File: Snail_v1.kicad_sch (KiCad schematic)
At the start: 18 parts, among them J1 PWM_Connector, U1 PAM8406D, U2 STM32G431K6Tx

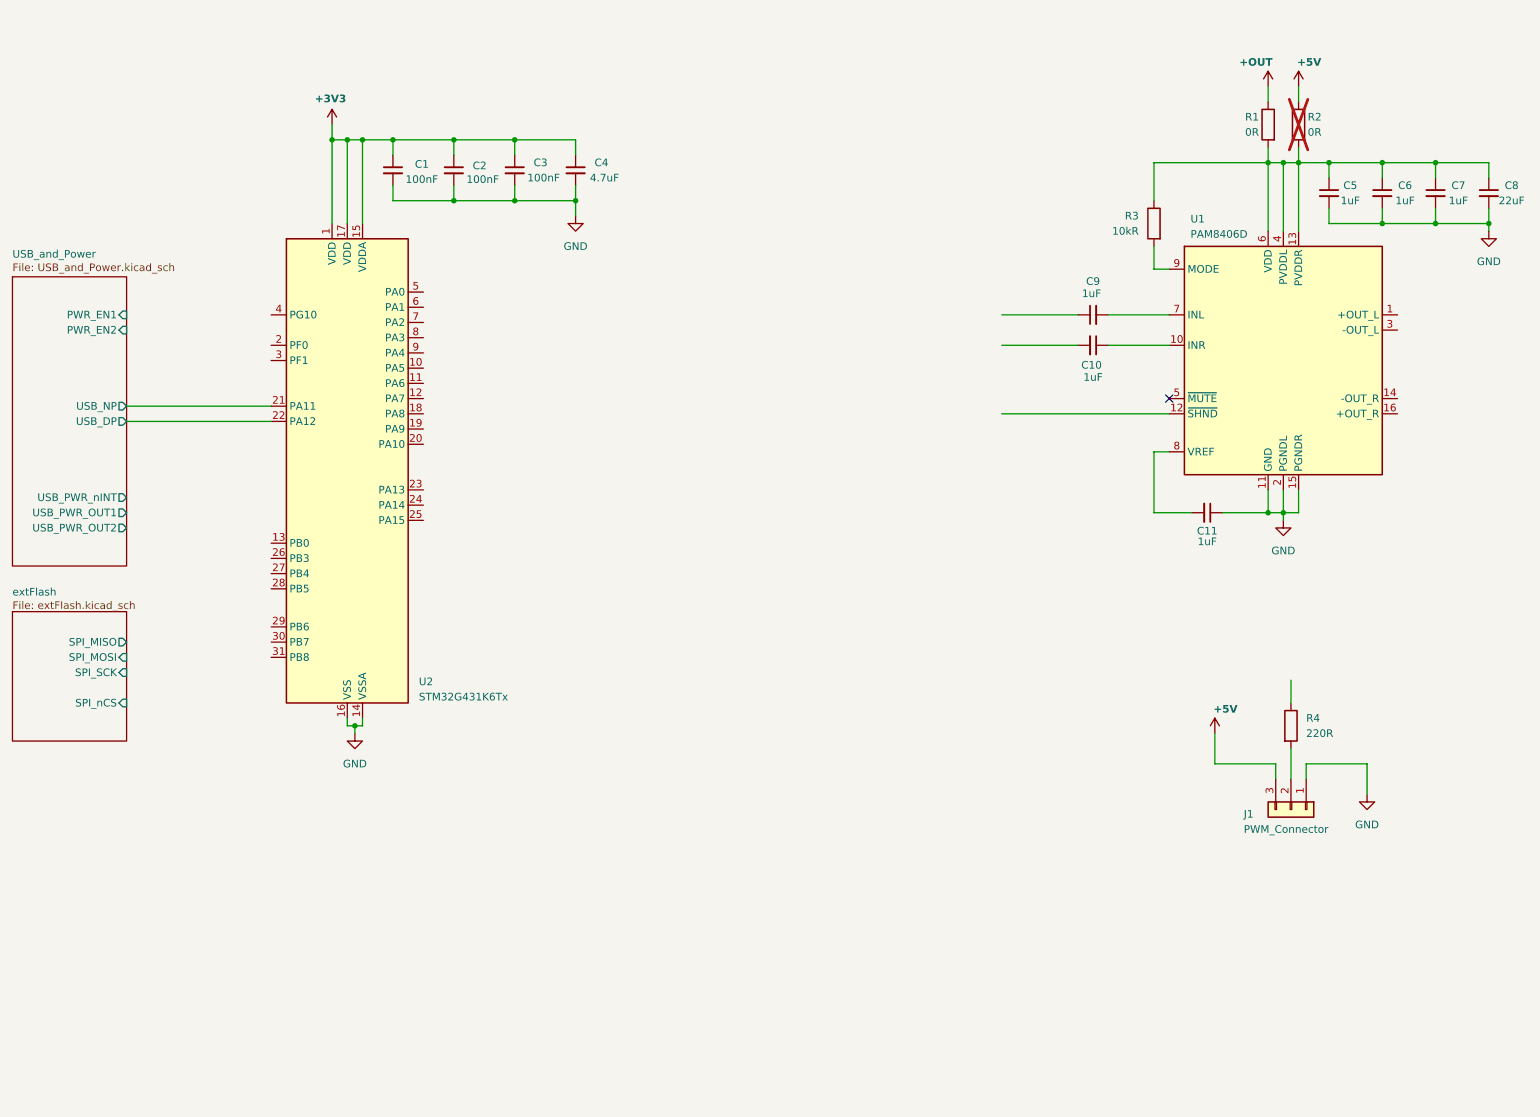
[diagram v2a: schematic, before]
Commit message: Added JDY-68A and replaced Amp-IC for PAM8302AAS
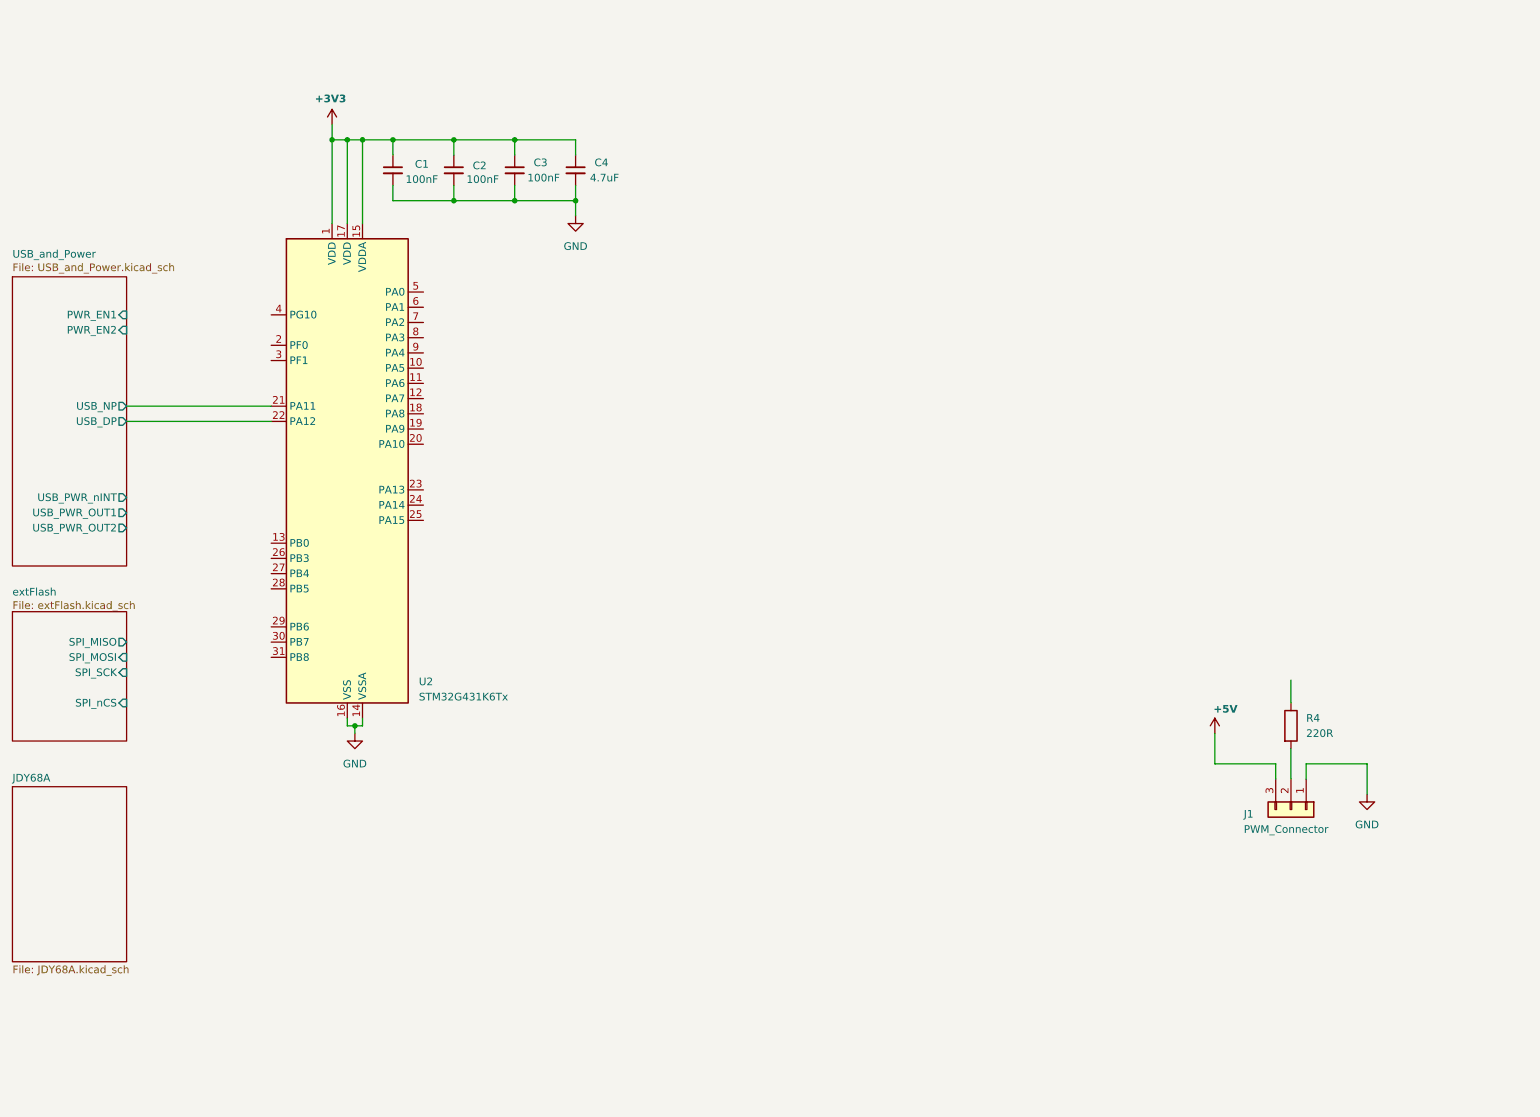
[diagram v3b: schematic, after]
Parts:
- removed C10, C11, C5, C6, C7, C9: 1uF, symbol Device:C_Small
- removed C8: 22uF, symbol Device:C_Small
- removed R1, R2: 0R, symbol Device:R
- removed R3: 10kR, symbol Device:R
- removed U1: PAM8406D, Package_SO:SOIC-16_3.9x9.9mm_P1.27mm, symbol Amplifier_Audio:PAM8406D
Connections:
- no-connect marks 1 -> 0
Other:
- added sheet JDY68A (JDY68A.kicad_sch)

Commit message: Changed LDO to Buc-Boost
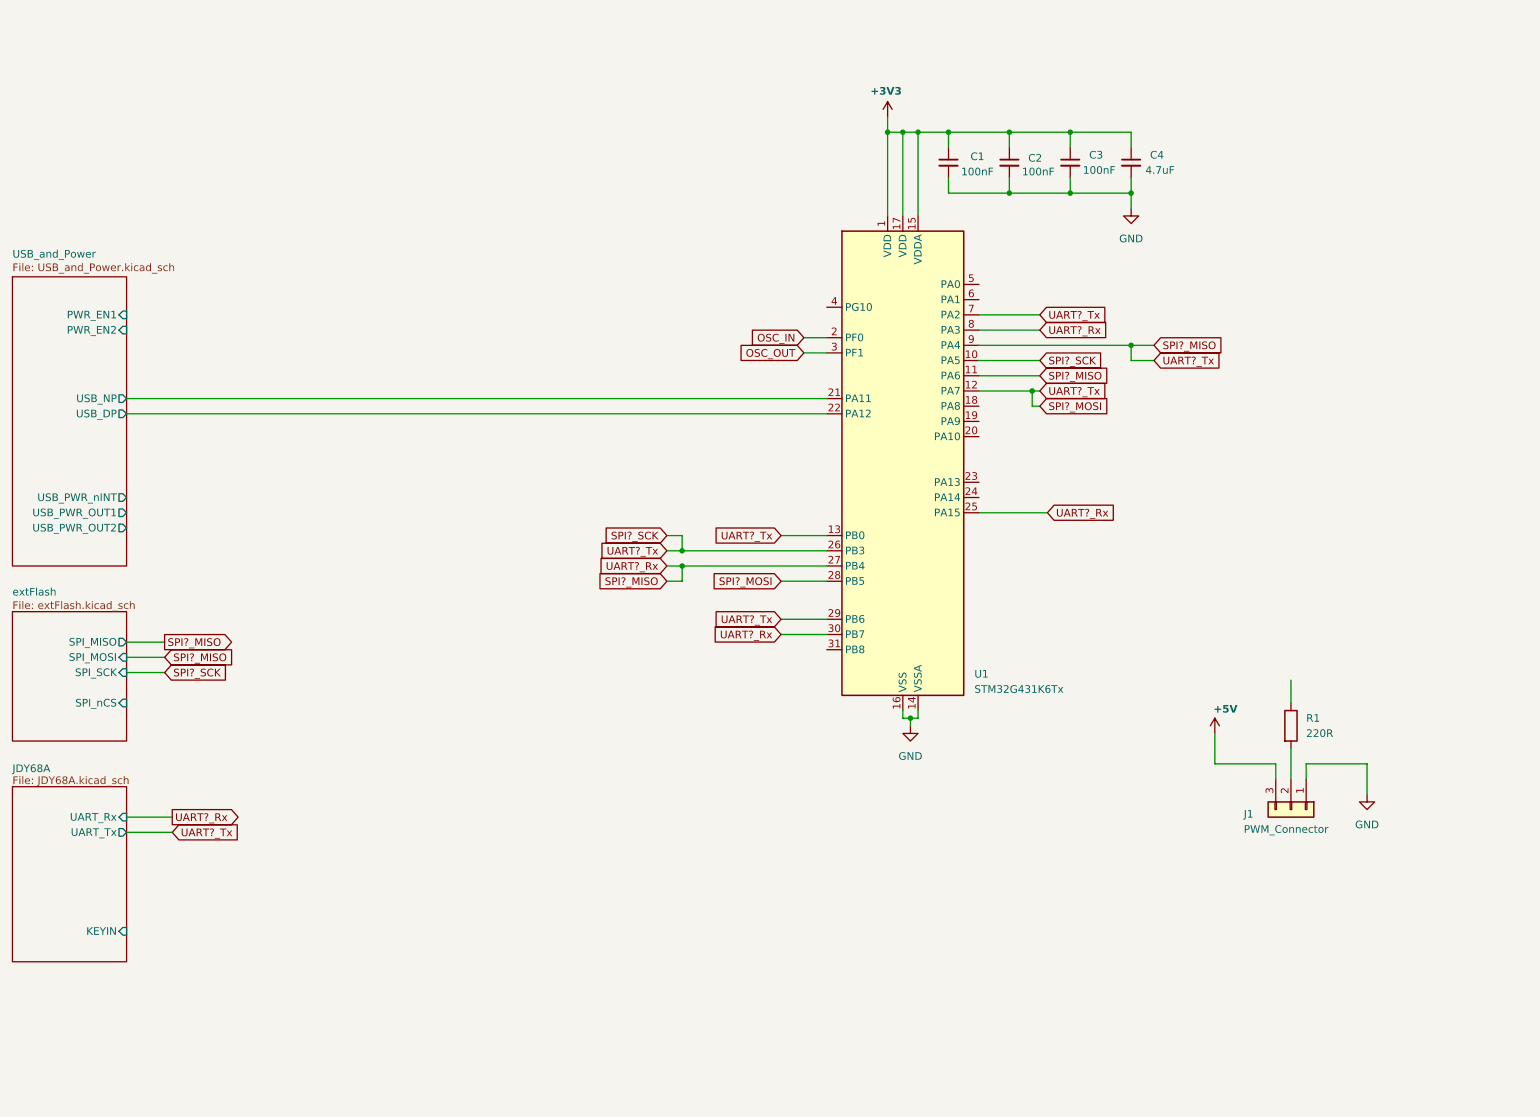
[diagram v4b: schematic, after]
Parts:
- C1, C2, C3, C4: footprint (none) -> Capacitor_SMD:C_0805_2012Metric_Pad1.18x1.45mm_HandSolder
- J1: footprint (none) -> Connector_PinHeader_2.54mm:PinHeader_1x03_P2.54mm_Vertical
- R1: renamed from R4; footprint (none) -> Resistor_SMD:R_0805_2012Metric_Pad1.20x1.40mm_HandSolder
- renumbered U2 to U1
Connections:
- net SPI?_MISO: now reaches U1.10 (PA5)
- net SPI?_MISO: now also U1.11 (PA6), U1.12 (PA7), U1.13 (PB0), U1.25 (PA15), U1.26 (PB3), U1.27 (PB4), U1.28 (PB5), U1.29 (PB6), U1.30 (PB7), U1.7 (PA2), U1.8 (PA3), U1.9 (PA4)
- net OSC_IN: now reaches U1.2 (PF0)
- net OSC_OUT: now reaches U1.3 (PF1)
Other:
- sheet JDY68A ports: added KEYIN, UART_Rx, UART_Tx; removed none
- moved on the sheet: C1, C2, C3, C4, U1

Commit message: Added LEDs + TPs
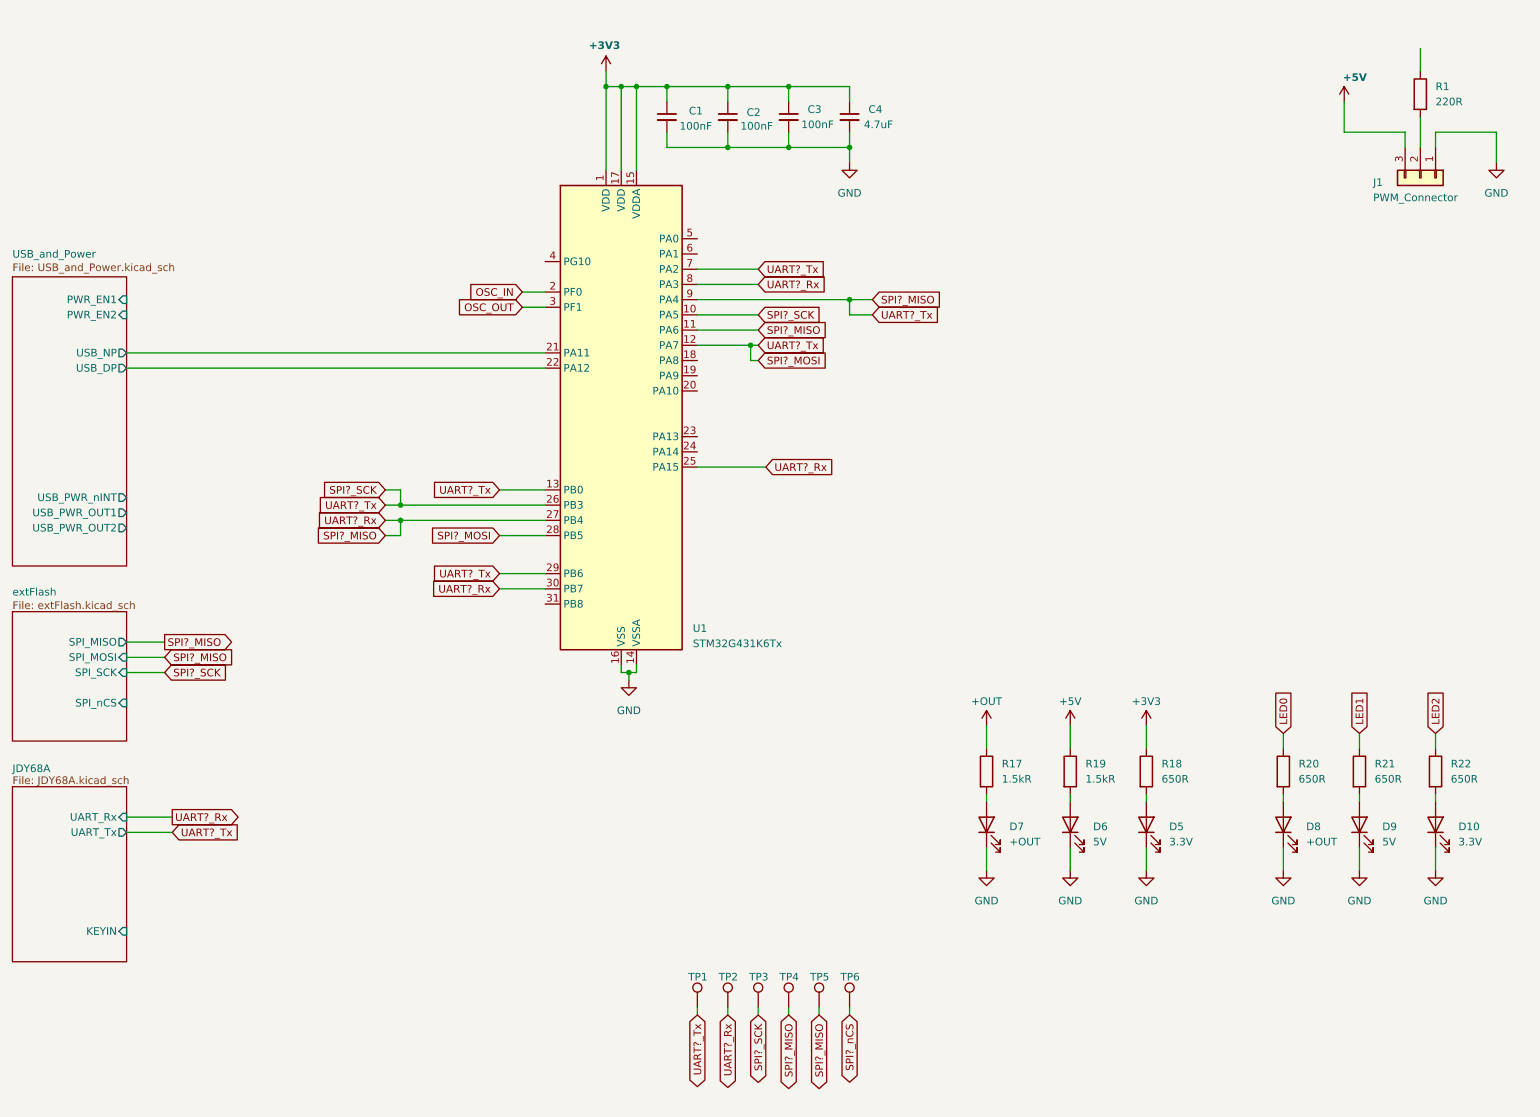
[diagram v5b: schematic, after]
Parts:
- added D10, D5: 3.3V, symbol Device:LED
- added D6, D9: 5V, symbol Device:LED
- added D7, D8: +OUT, symbol Device:LED
- added R17, R19: 1.5kR, symbol Device:R
- added R18, R20, R21, R22: 650R, symbol Device:R
- added TP1, TP2, TP3, TP4, TP5, TP6: TestPoint, symbol Connector:TestPoint
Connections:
- net +3V3: now also R18.1
- net +5V: now also R19.1
- net GND: now also D10.1 (K), D5.1 (K), D6.1 (K), D7.1 (K), D8.1 (K), D9.1 (K)
- net SPI?_MISO: now also TP1.1, TP2.1, TP3.1, TP4.1, TP5.1
- new net: D7.2 (A), R17.2
- new net: D5.2 (A), R18.2
- new net: D9.2 (A), R21.2
- new net: D10.2 (A), R22.2
- new net: D6.2 (A), R19.2
- new net: D8.2 (A), R20.2
- new net +OUT: R17.1
- new net LED0: R20.1
- new net LED1: R21.1
- new net LED2: R22.1
- new net SPI?_nCS: TP6.1
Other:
- moved on the sheet: C1, C2, C3, C4, J1, R1, U1

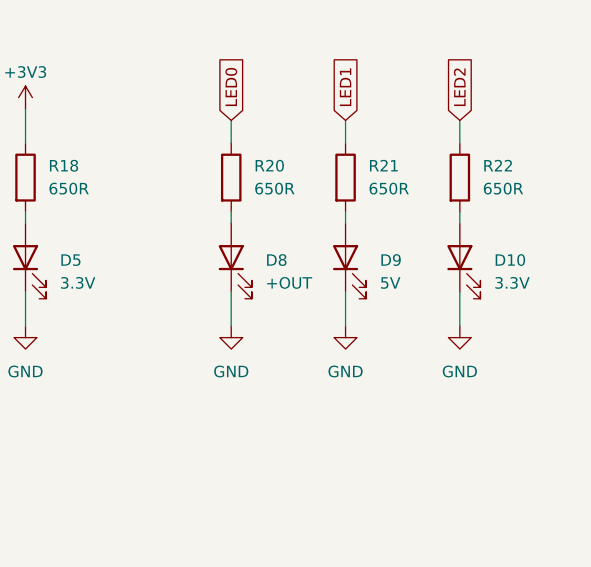
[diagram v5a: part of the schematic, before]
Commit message: Added missing footprints
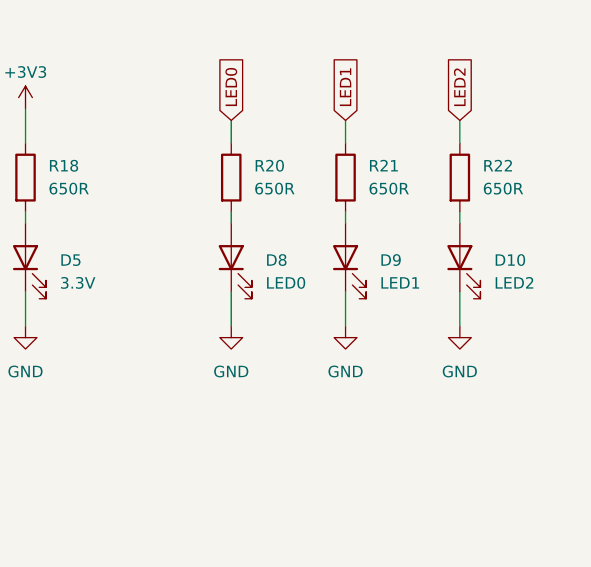
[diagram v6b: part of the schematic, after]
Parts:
- D10: value 3.3V -> LED2; footprint (none) -> LED_SMD:LED_0805_2012Metric_Pad1.15x1.40mm_HandSolder
- D5, D6, D7: footprint (none) -> LED_SMD:LED_0805_2012Metric_Pad1.15x1.40mm_HandSolder
- D8: value +OUT -> LED0; footprint (none) -> LED_SMD:LED_0805_2012Metric_Pad1.15x1.40mm_HandSolder
- D9: value 5V -> LED1; footprint (none) -> LED_SMD:LED_0805_2012Metric_Pad1.15x1.40mm_HandSolder
- R17, R18, R19, R20, R21, R22: footprint (none) -> Resistor_SMD:R_0805_2012Metric_Pad1.20x1.40mm_HandSolder
- TP1, TP2, TP3, TP4, TP5, TP6: footprint (none) -> TestPoint:TestPoint_Pad_D2.5mm
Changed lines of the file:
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@@
 			)
 		)
-		(property "Footprint" ""
+		(property "Footprint" "Resistor_SMD:R_0805_2012Metric_Pad1.20x1.40mm_HandSolder"
 			(at 187.452 138.43 90)
 			(effects
@@
 			)
 		)
-		(property "Footprint" ""
+		(property "Footprint" "LED_SMD:LED_0805_2012Metric_Pad1.15x1.40mm_HandSolder"
 			(at 215.9 147.32 0)
 			(effects
@@
 			)
 		)
-		(property "Footprint" ""
+		(property "Footprint" "Resistor_SMD:R_0805_2012Metric_Pad1.20x1.40mm_HandSolder"
 			(at 249.682 138.43 90)
 			(effects
@@
 			)
 		)
-		(property "Footprint" ""
+		(property "Footprint" "Resistor_SMD:R_0805_2012Metric_Pad1.20x1.40mm_HandSolder"
 			(at 262.382 138.43 90)
 			(effects
@@
 			)
 		)
-		(property "Footprint" ""
+		(property "Footprint" "TestPoint:TestPoint_Pad_D2.5mm"
 			(at 151.13 177.8 0)
 			(effects
@@
 			)
 		)
-		(property "Footprint" ""
+		(property "Footprint" "TestPoint:TestPoint_Pad_D2.5mm"
 			(at 161.29 177.8 0)
 			(effects
@@
 			)
 		)
-		(property "Footprint" ""
+		(property "Footprint" "TestPoint:TestPoint_Pad_D2.5mm"
 			(at 166.37 177.8 0)
 			(effects
@@
 			)
 		)
-		(property "Value" "3.3V"
+		(property "Value" "LED2"
 			(at 267.97 150.1774 90)
 			(effects
@@
 			)
 		)
-		(property "Footprint" ""
+		(property "Footprint" "LED_SMD:LED_0805_2012Metric_Pad1.15x1.40mm_HandSolder"
 			(at 264.16 147.32 0)
 			(effects
@@
 			)
 		)
-		(property "Footprint" ""
+		(property "Footprint" "LED_SMD:LED_0805_2012Metric_Pad1.15x1.40mm_HandSolder"
 			(at 203.2 147.32 0)
 			(effects
@@
 			)
 		)
-		(property "Footprint" ""
+		(property "Footprint" "LED_SMD:LED_0805_2012Metric_Pad1.15x1.40mm_HandSolder"
 			(at 189.23 147.32 0)
 			(effects
@@
 			)
 		)
-		(property "Footprint" ""
+		(property "Footprint" "Resistor_SMD:R_0805_2012Metric_Pad1.20x1.40mm_HandSolder"
 			(at 214.122 138.43 90)
 			(effects
@@
 			)
 		)
-		(property "Footprint" ""
+		(property "Footprint" "Resistor_SMD:R_0805_2012Metric_Pad1.20x1.40mm_HandSolder"
 			(at 236.982 138.43 90)
 			(effects
@@
 			)
 		)
-		(property "Value" "5V"
+		(property "Value" "LED1"
 			(at 255.27 150.1774 90)
 			(effects
@@
 			)
 		)
-		(property "Footprint" ""
+		(property "Footprint" "LED_SMD:LED_0805_2012Metric_Pad1.15x1.40mm_HandSolder"
 			(at 251.46 147.32 0)
 			(effects
@@
 			)
 		)
-		(property "Footprint" ""
+		(property "Footprint" "TestPoint:TestPoint_Pad_D2.5mm"
 			(at 156.21 177.8 0)
 			(effects
@@
 			)
 		)
-		(property "Footprint" ""
+		(property "Footprint" "Resistor_SMD:R_0805_2012Metric_Pad1.20x1.40mm_HandSolder"
 			(at 201.422 138.43 90)
 			(effects
@@
 			)
 		)
-		(property "Footprint" ""
+		(property "Footprint" "TestPoint:TestPoint_Pad_D2.5mm"
 			(at 146.05 177.8 0)
 			(effects
@@
 			)
 		)
-		(property "Value" "+OUT"
+		(property "Value" "LED0"
 			(at 242.57 150.1774 90)
 			(effects
@@
 			)
 		)
-		(property "Footprint" ""
+		(property "Footprint" "LED_SMD:LED_0805_2012Metric_Pad1.15x1.40mm_HandSolder"
 			(at 238.76 147.32 0)
 			(effects
@@
 			)
 		)
-		(property "Footprint" ""
+		(property "Footprint" "TestPoint:TestPoint_Pad_D2.5mm"
 			(at 171.45 177.8 0)
 			(effects

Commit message: Started with layout
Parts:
- added C22: 830059539, KiCad:830059539, symbol 830059539:830059539
- added C23, C24: 33pF, Capacitor_SMD:C_0805_2012Metric_Pad1.18x1.45mm_HandSolder, symbol Device:C
- added J5: Conn_ARM_SWD_TagConnect_TC2030-NL, Connector:Tag-Connect_TC2030-IDC-NL_2x03_P1.27mm_Vertical, symbol Connector:Conn_ARM_SWD_TagConnect_TC2030-NL
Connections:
- net +3V3: now also J5.1 (VCC)
- net GND: now also C22.2 (GND), C22.4 (GND), C23.2, C24.2, J5.5 (GND)
- net OSC_IN: now also C22.1 (CRYSTAL_1), C23.1
- net OSC_OUT: now also C22.3 (CRYSTAL_2), C24.1
- net USB_and_Power/PWR_EN1: now also U1.19 (PA9)
- net USB_and_Power/PWR_EN2: now also U1.18 (PA8)
- net SWDIO: now reaches U1.23 (PA13)
- net SWDIO: now also J5.2 (SWDIO)
- net SWCLK: now reaches U1.24 (PA14)
- net SWCLK: now also J5.4 (SWCLK)
- net nRST: now reaches U1.4 (PG10)
- net nRST: now also J5.3 (~{RESET})
- net USB_and_Power/USB_DP renamed USB_and_Power/USB+
- net USB_and_Power/USB_NP renamed USB_and_Power/USB-
- no-connect marks 0 -> 1
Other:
- sheet USB_and_Power ports: added 5V_EN, USB+, USB-; removed USB_DP, USB_NP
